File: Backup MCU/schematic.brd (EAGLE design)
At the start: 55 x 60 mm, 14 parts, among them T1 2N2222

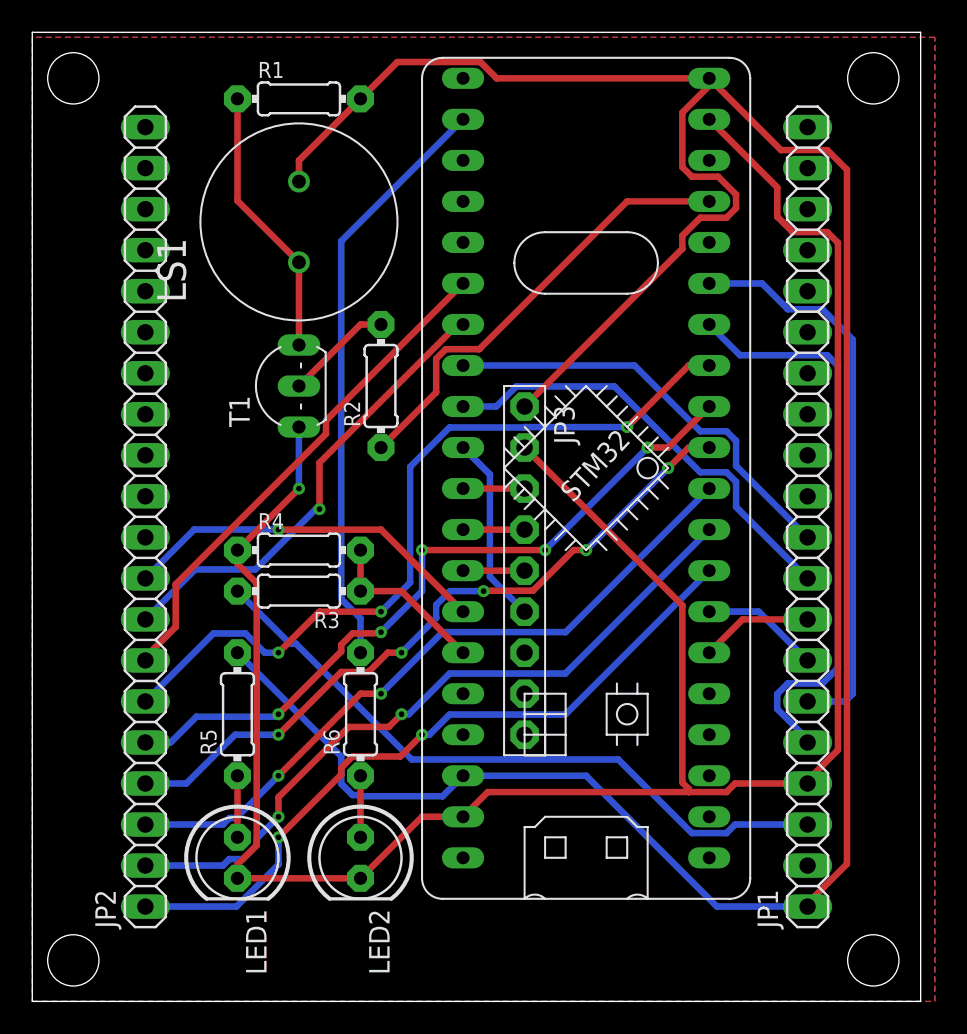
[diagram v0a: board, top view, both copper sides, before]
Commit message: Additional changes for backup MCU
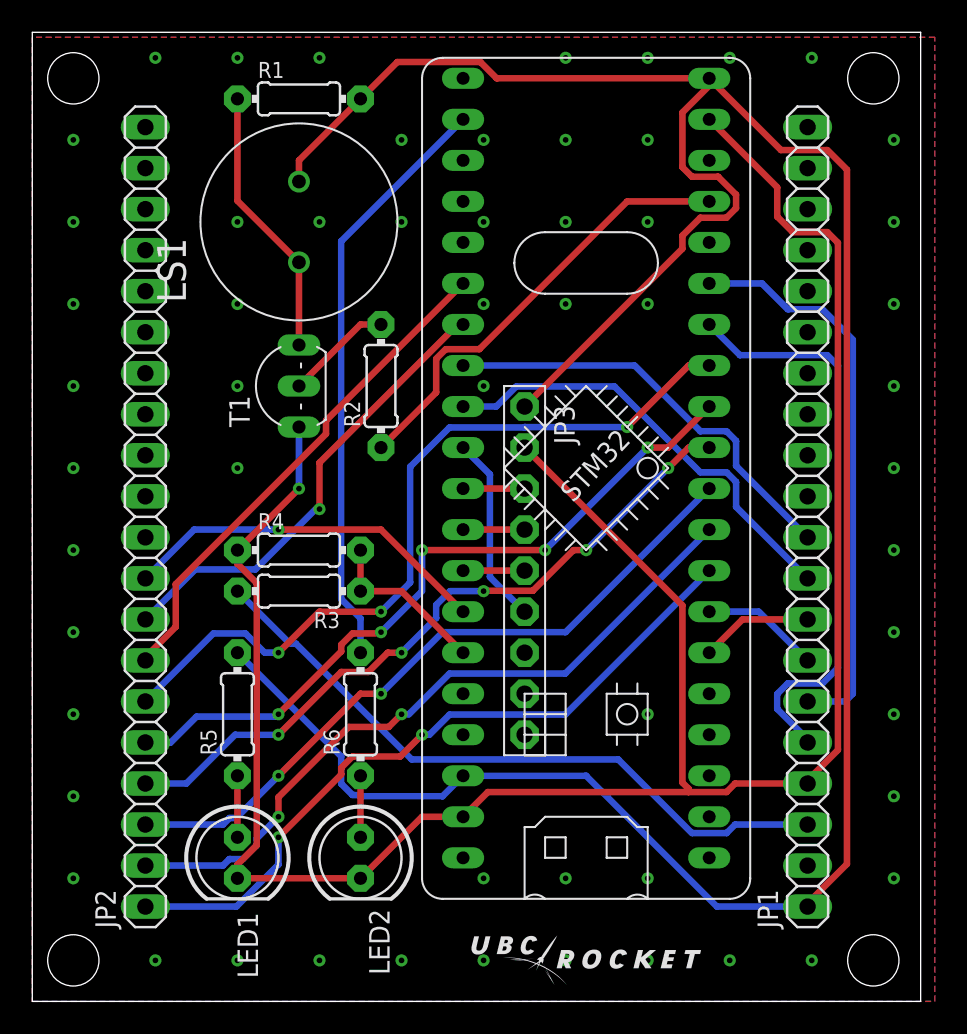
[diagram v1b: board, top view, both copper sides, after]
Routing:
- net GND: vias 1 -> 57
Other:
- board text added: "C:/Users/callu/Documents/UBC Rocket/2022 Avionics/image_monochrome.bmp"
